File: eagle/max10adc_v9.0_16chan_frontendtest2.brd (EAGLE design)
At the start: 167 x 79 mm, 189 parts, among them IC1 MAX11115AUT+T, IC2 MAX11115AUT+T, IC3 OPA4322AIPWR, IC4 MAX11115AUT+T, IC5 MAX11115AUT+T, K1 AQY21SOP, K3 AQY21SOP, K5 AQY21SOP, K6 AQY21SOP, U340G CH340G, X1 LTI-SASF54GT, X4 LTI-SASF54GT, X5 LTI-SASF54GT, X6 LTI-SASF54GT, Y1 ABL-12.000MHZ-B2

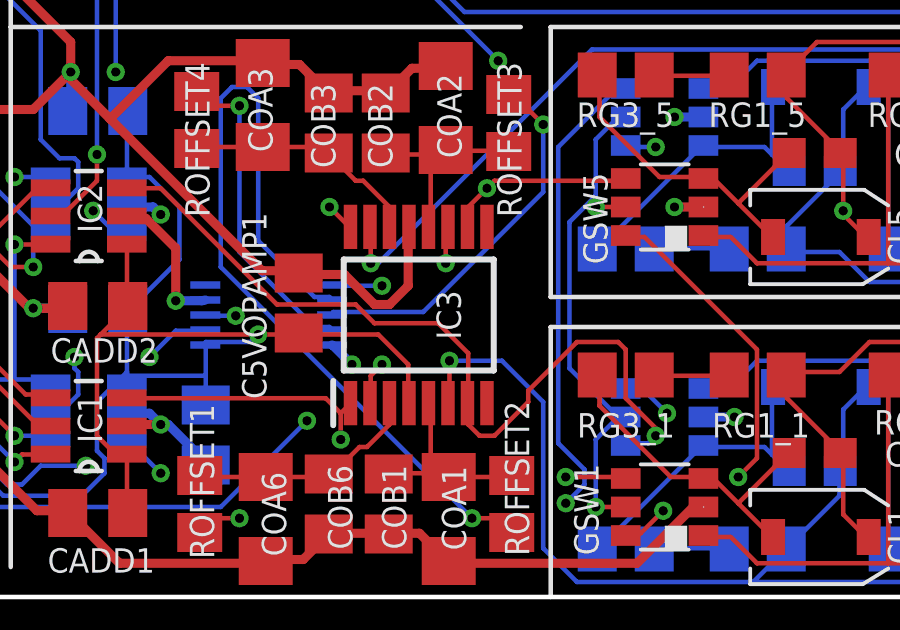
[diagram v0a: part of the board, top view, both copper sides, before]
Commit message: 2msps working
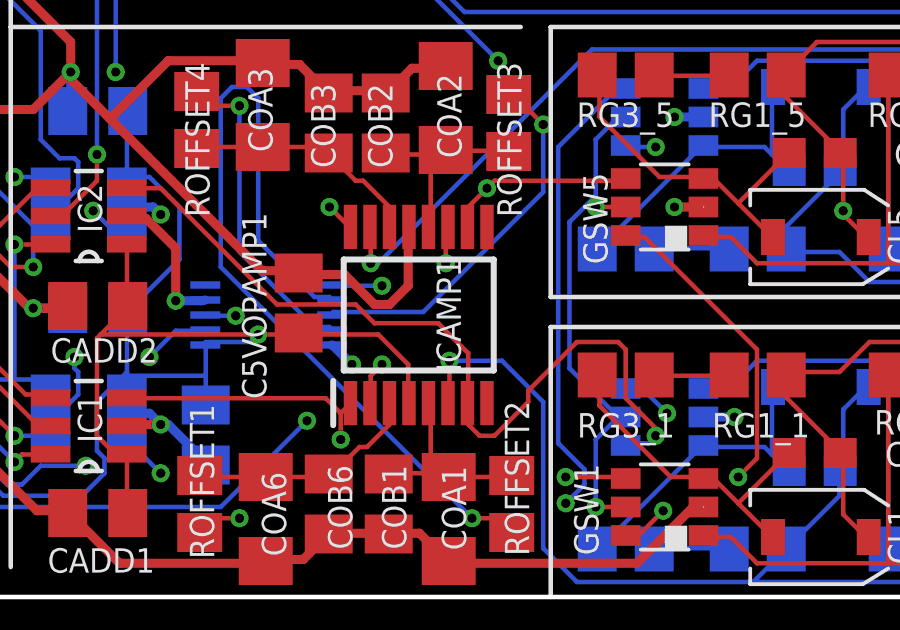
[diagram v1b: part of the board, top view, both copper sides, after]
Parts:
- removed IC5: MAX11115AUT+T, SamacSys_Parts:SOT95P280X145-6N
- added ICAMP1: OPA4322AIPWR, SamacSys_Parts:SOP65P640X120-16N
- IC3: value OPA4322AIPWR -> MAX11115AUT+T; device SamacSys_Parts:SOP65P640X120-16N -> SamacSys_Parts:SOT95P280X145-6N
- moved IC3 11.5 mm to (52.6, -5.80), flipped to the bottom, turned to 0 degrees
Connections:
- net CLKOUT_32: now also IC3.4; no longer IC5.4
- net CLKOUT_33: now also IC3.6; no longer IC5.6
- net D2A: now also IC3.5; no longer IC5.5
- net GND: now also IC3.2, ICAMP1.13; no longer IC3.13, IC5.2
- net INA1: now also ICAMP1.1; no longer IC3.1
- net INA2: now also ICAMP1.7; no longer IC3.7
- net INA3: now also IC3.3, ICAMP1.10; no longer IC3.10, IC5.3
- net INA4: now also ICAMP1.16; no longer IC3.16
- net INAMINUS1: now also ICAMP1.2; no longer IC3.2
- net INAMINUS2: now also ICAMP1.6; no longer IC3.6
- net INAMINUS3: now also ICAMP1.11; no longer IC3.11
- net INAMINUS4: now also ICAMP1.15; no longer IC3.15
- net OFFSET1: now also ICAMP1.3; no longer IC3.3
- net OFFSET2: now also ICAMP1.5; no longer IC3.5
- net OFFSET3: now also ICAMP1.12; no longer IC3.12
- net OFFSET4: now also ICAMP1.14; no longer IC3.14
- net VCCA: now also IC3.1, ICAMP1.4; no longer IC3.4, IC5.1
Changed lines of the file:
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@@
 <drawing>
 <settings>
-<setting alwaysvectorfont="yes"/>
+<setting alwaysvectorfont="no"/>
 <setting keepoldvectorfont="yes"/>
 <setting verticaltext="up"/>
@@
 <attribute name="NAME" x="45.4" y="58.75" size="0.8128" layer="25" ratio="18" rot="R180"/>
 </element>
-<element name="IC3" library="SamacSys_Parts" package="SOP65P640X120-16N" value="OPA4322AIPWR" x="63.6" y="-2.6" smashed="yes" rot="R90">
+<element name="ICAMP1" library="SamacSys_Parts" package="SOP65P640X120-16N" value="OPA4322AIPWR" x="63.6" y="-2.6" smashed="yes" rot="R90">
 <attribute name="DESCRIPTION" value="20MHz, Low Noise, 1.8V, RRIO, CMOS Operational Amplifier" x="63.6" y="-2.6" size="1.778" layer="27" rot="R90" display="off"/>
 <attribute name="HEIGHT" value="1.2mm" x="63.6" y="-2.6" size="1.778" layer="27" rot="R90" display="off"/>
@@
 <attribute name="NAME" x="54.9" y="5.175" size="0.8128" layer="26" font="vector" rot="MR0"/>
 </element>
-<element name="IC5" library="SamacSys_Parts" package="SOT95P280X145-6N" value="MAX11115AUT+T" x="52.6" y="-5.8" smashed="yes" rot="MR0">
+<element name="IC3" library="SamacSys_Parts" package="SOT95P280X145-6N" value="MAX11115AUT+T" x="52.6" y="-5.8" smashed="yes" rot="MR0">
 <attribute name="DESCRIPTION" value="ADC" x="56.6" y="-10.8" size="1.778" layer="28" rot="MR0" display="off"/>
 <attribute name="HEIGHT" value="mm" x="56.6" y="-10.8" size="1.778" layer="28" rot="MR0" display="off"/>
@@
 <contactref element="S1" pad="6"/>
 <contactref element="S2" pad="6"/>
-<contactref element="IC3" pad="13"/>
+<contactref element="ICAMP1" pad="13"/>
 <contactref element="IC4" pad="2"/>
 <contactref element="CADD1" pad="2"/>
@@
 <contactref element="IC2" pad="2"/>
 <contactref element="CADD3" pad="2"/>
-<contactref element="IC5" pad="2"/>
+<contactref element="IC3" pad="2"/>
 <contactref element="CADD4" pad="2"/>
 <contactref element="IOEXPAND_0X22" pad="10"/>
@@
 <contactref element="IC1" pad="6"/>
 <contactref element="IC2" pad="6"/>
-<contactref element="IC5" pad="6"/>
+<contactref element="IC3" pad="6"/>
 <wire x1="38.125" y1="18.75" x2="38.125" y2="19.375" width="0.1524" layer="1"/>
 <wire x1="37.5" y1="18.125" x2="38.125" y2="18.75" width="0.1524" layer="1"/>
@@
 <signal name="D2A">
 <contactref element="FPGA" pad="45"/>
-<contactref element="IC5" pad="5"/>
+<contactref element="IC3" pad="5"/>
 <wire x1="40.75" y1="25.5" x2="41.625" y2="25.5" width="0.1524" layer="1"/>
 <wire x1="42" y1="25.5" x2="40.75" y2="25.5" width="0.1524" layer="16"/>
@@
 <signal name="INA1">
 <contactref element="GSW1" pad="4"/>
-<contactref element="IC3" pad="1"/>
+<contactref element="ICAMP1" pad="1"/>
 <contactref element="IC1" pad="3"/>
 <wire x1="68.5" y1="-8" x2="70.5" y2="-8" width="0.1524" layer="1"/>
@@
 <contactref element="IC1" pad="4"/>
 <contactref element="IC2" pad="4"/>
-<contactref element="IC5" pad="4"/>
+<contactref element="IC3" pad="4"/>
 <wire x1="37.75" y1="20.25" x2="37.75" y2="19.5" width="0.1524" layer="1"/>
 <wire x1="37.875" y1="20.375" x2="37.75" y2="20.25" width="0.1524" layer="1"/>
@@
 <contactref element="RIN1" pad="2"/>
 <contactref element="CIN1" pad="2"/>
-<contactref element="IC3" pad="2"/>
+<contactref element="ICAMP1" pad="2"/>
 <wire x1="77.75" y1="-9.25" x2="77.75" y2="-7.25" width="0.1524" layer="1"/>
 <wire x1="78.5" y1="-10" x2="77.75" y2="-9.25" width="0.1524" layer="1"/>
@@
 <contactref element="ROFFSET1" pad="1"/>
 <contactref element="COA6" pad="2"/>
-<contactref element="IC3" pad="3"/>
+<contactref element="ICAMP1" pad="3"/>
 <wire x1="58.5" y1="-8" x2="56.375" y2="-8" width="0.1524" layer="1"/>
 <wire x1="56.375" y1="-8" x2="56.3" y2="-7.95" width="0.1524" layer="1"/>
@@
 <contactref element="DAC1" pad="1"/>
 <contactref element="COFFSET" pad="2"/>
-<contactref element="IC3" pad="4"/>
+<contactref element="ICAMP1" pad="4"/>
 <contactref element="IC4" pad="1"/>
 <contactref element="CADD1" pad="1"/>
@@
 <contactref element="IC2" pad="1"/>
 <contactref element="CADD3" pad="1"/>
-<contactref element="IC5" pad="1"/>
+<contactref element="IC3" pad="1"/>
 <contactref element="CADD4" pad="1"/>
 <wire x1="45.625" y1="1" x2="48.2" y2="1" width="0.1524" layer="1"/>
@@
 <signal name="INA2">
 <contactref element="GSW3" pad="4"/>
-<contactref element="IC3" pad="7"/>
+<contactref element="ICAMP1" pad="7"/>
 <contactref element="IC2" pad="3"/>
 <wire x1="71.25" y1="-6.875" x2="70.5" y2="-6.875" width="0.1524" layer="16"/>
@@
 <contactref element="RIN3" pad="2"/>
 <contactref element="CIN3" pad="2"/>
-<contactref element="IC3" pad="6"/>
+<contactref element="ICAMP1" pad="6"/>
 <wire x1="95.5" y1="-6.375" x2="95.5" y2="-8.75" width="0.1524" layer="16"/>
 <wire x1="95.5" y1="-8.75" x2="95.4" y2="-8.75" width="0.1524" layer="16"/>
@@
 <signal name="INA3">
 <contactref element="GSW5" pad="4"/>
-<contactref element="IC3" pad="10"/>
-<contactref element="IC5" pad="3"/>
+<contactref element="ICAMP1" pad="10"/>
+<contactref element="IC3" pad="3"/>
 <wire x1="66.125" y1="1.875" x2="70.5" y2="1.875" width="0.1524" layer="1"/>
 <wire x1="65.25" y1="1" x2="65.875" y2="1.625" width="0.1524" layer="1"/>
@@
 <contactref element="RIN5" pad="2"/>
 <contactref element="CIN5" pad="2"/>
-<contactref element="IC3" pad="11"/>
+<contactref element="ICAMP1" pad="11"/>
 <wire x1="95.5" y1="3.75" x2="95.5" y2="1.375" width="0.1524" layer="1"/>
 <wire x1="95.5" y1="1.375" x2="95.4" y2="1.35" width="0.1524" layer="1"/>
@@
 <signal name="INA4">
 <contactref element="GSW6" pad="4"/>
-<contactref element="IC3" pad="16"/>
+<contactref element="ICAMP1" pad="16"/>
 <contactref element="IC4" pad="3"/>
 <wire x1="71.5" y1="3" x2="70.5" y2="3" width="0.1524" layer="16"/>
@@
 <contactref element="RIN6" pad="2"/>
 <contactref element="CIN6" pad="2"/>
-<contactref element="IC3" pad="15"/>
+<contactref element="ICAMP1" pad="15"/>
 <wire x1="77.75" y1="4.25" x2="77.75" y2="2.25" width="0.1524" layer="16"/>
 <wire x1="78.5" y1="5" x2="77.75" y2="4.25" width="0.1524" layer="16"/>
@@
 <contactref element="COB3" pad="2"/>
 <contactref element="COA3" pad="2"/>
-<contactref element="IC3" pad="14"/>
+<contactref element="ICAMP1" pad="14"/>
 <wire x1="58.4" y1="3" x2="56.25" y2="3" width="0.1524" layer="1"/>
 <wire x1="56.25" y1="3" x2="56.2" y2="2.95" width="0.1524" layer="1"/>
@@
 <contactref element="COB2" pad="2"/>
 <contactref element="COA2" pad="2"/>
-<contactref element="IC3" pad="12"/>
+<contactref element="ICAMP1" pad="12"/>
 <wire x1="64" y1="2.375" x2="64" y2="0.375" width="0.1524" layer="1"/>
 <wire x1="64.5" y1="2.875" x2="64.375" y2="2.75" width="0.1524" layer="1"/>
@@
 <contactref element="COB1" pad="2"/>
 <contactref element="COA1" pad="2"/>
-<contactref element="IC3" pad="5"/>
+<contactref element="ICAMP1" pad="5"/>
 <wire x1="64" y1="-7.5" x2="64" y2="-5.625" width="0.1524" layer="1"/>
 <wire x1="64.5" y1="-8" x2="64.375" y2="-7.875" width="0.1524" layer="1"/>

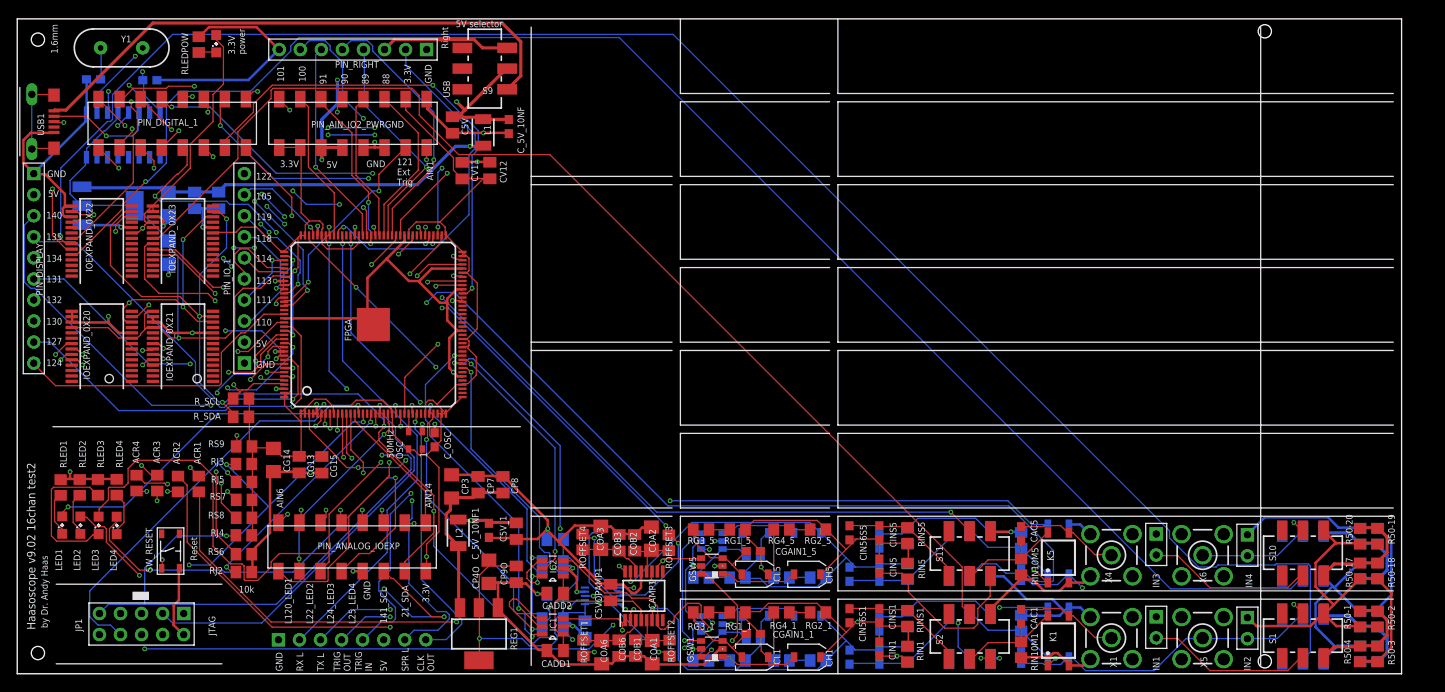
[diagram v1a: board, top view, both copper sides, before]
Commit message: 4x less gain and associated compensation, and input 6 pin connector
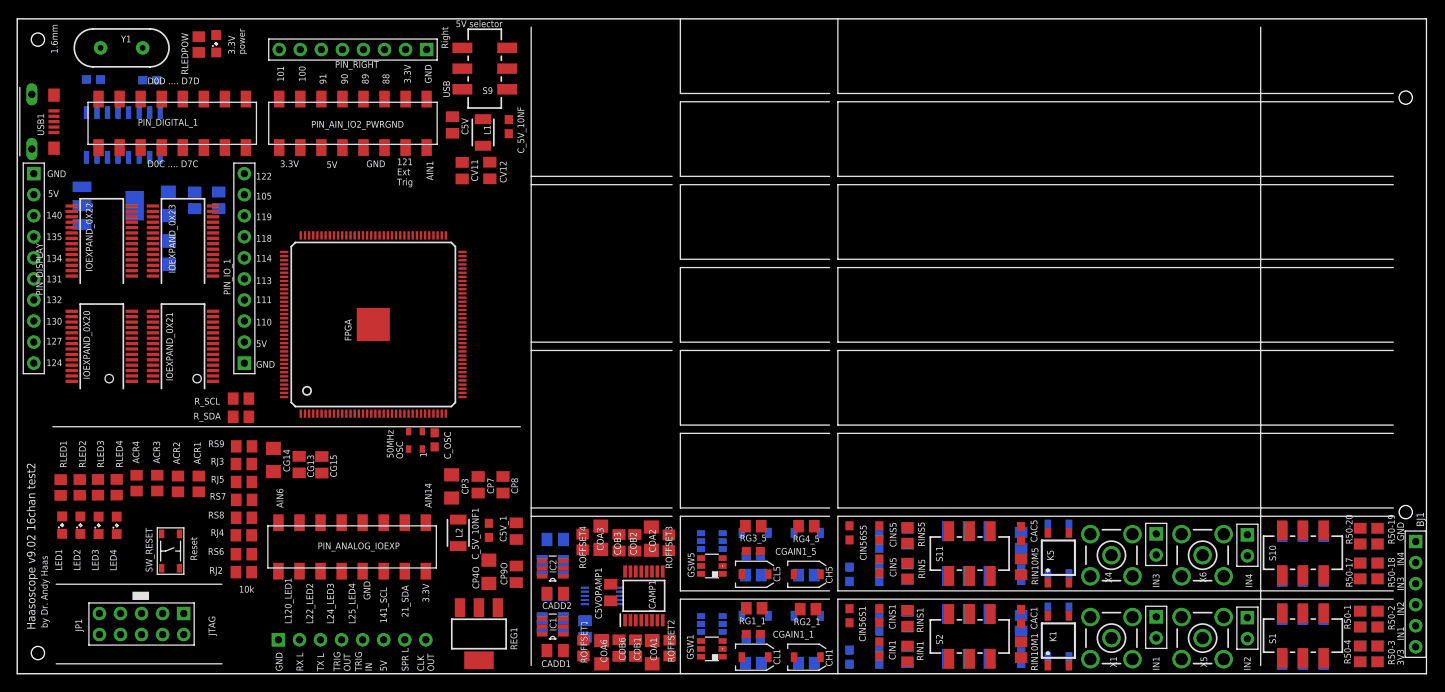
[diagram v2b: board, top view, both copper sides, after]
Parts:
- removed RG1_5, RG1_6, RG3_1, RG3_3: 100k, resistor:R0805
- removed RG2_5, RG2_6, RG4_1, RG4_3: 1M, resistor:R0805
- added BJ1: 6p-2.54, Seeed-Connector:H6-2.54
- CGAIN1_1, CGAIN1_3, CGAIN1_5, CGAIN1_6: value 33pF -> 220pF
- CH1, CH3, CH5, CH6: value 3-10pF -> 8-45pF
- RG1_1, RG1_3, RG3_5, RG3_6: value 100k -> 47k
- RG2_1, RG2_3, RG4_5, RG4_6: value 1M -> 470k
- moved RG3_5 6.31 mm to (76.8, 5.80)
- moved RG3_6 6.31 mm to (76.8, -0.10)
- moved RG4_5 3.03 mm to (83.2, 5.80)
- moved RG4_6 3.01 mm to (83.2, -0.10)
- moved RG1_1 2.06 mm to (76.9, -4.10)
- moved RG1_3 1.92 mm to (76.8, -10.7)
- moved RG2_3 1.43 mm to (83.2, -10.7)
- moved RG2_1 1.26 mm to (83.4, -4.20)
- moved S13 0.20 mm to (102.7, 2.50)
- moved S6 0.20 mm to (102.7, -7.50)
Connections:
- removed net INJ5: CAC5.2, IN3.2, K5.3, S10.2, X4.1
- removed net INJ6: CAC6.2, IN4.2, K6.3, S12.2, X6.1
- removed net N$2: RG1_1.1, RG3_1.2
- removed net N$20: RG1_5.1, RG3_5.2
- removed net N$21: RG2_5.1, RG4_5.2
- removed net N$25: RG1_6.1, RG3_6.2
- removed net N$26: RG2_6.1, RG4_6.2
- removed net N$3: RG2_1.1, RG4_1.2
- removed net N$7: RG1_3.1, RG3_3.2
- removed net N$8: RG2_3.1, RG4_3.2
- new net INJ2: BJ1.4, CAC3.2, IN2.2, K3.3, S5.2, X5.1
- new net INJ4: BJ1.2, CAC6.2, IN4.2, K6.3, S12.2, X6.1
- net CGAIN1: now also RG1_1.1; no longer RG3_1.1
- net CGAIN2: now also RG2_1.1; no longer RG4_1.1
- net CGAIN5: now also RG1_3.1; no longer RG3_3.1
- net CGAIN6: now also RG2_3.1; no longer RG4_3.1
- net GND: now also BJ1.1
- net INAMINUS3: now also RG3_5.2, RG4_5.2; no longer RG1_5.2, RG2_5.2
- net INAMINUS4: now also RG3_6.2, RG4_6.2; no longer RG1_6.2, RG2_6.2
- net INJ1: now also BJ1.5
- net INJ3: now also BJ1.3, CAC5.2, IN3.2, K5.3, S10.2, X4.1; no longer CAC3.2, IN2.2, K3.3, S5.2, X5.1
- net VCCA: now also BJ1.6
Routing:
- net GND: track 497.6 -> 0.00 mm, vias 33 -> 0
- net +3V3: track 364.8 -> 0.00 mm, vias 7 -> 0
- net E_50SW2: track 208.3 -> 0.00 mm, vias 1 -> 0
- net E_50SW3: track 198.9 -> 0.00 mm, vias 2 -> 0
- net E_50SW1: track 193.5 -> 0.00 mm, vias 2 -> 0
- net E_50SW4: track 192.3 -> 0.00 mm, vias 1 -> 0
- net +5V: track 163.8 -> 0.00 mm, vias 4 -> 0
- net L141_SCL: track 157.6 -> 0.00 mm, vias 8 -> 0
- net N$6: track 144.4 -> 0.00 mm, vias 2 -> 0
- net E_SS4: track 139.8 -> 0.00 mm, vias 2 -> 0
- net E_SS1: track 139.0 -> 0.00 mm
- net L21_SDA: track 138.6 -> 0.00 mm, vias 8 -> 0
- net N$5: track 138.0 -> 0.00 mm, vias 4 -> 0
- net N$11: track 128.0 -> 0.00 mm, vias 2 -> 0
- net N$4: track 127.4 -> 0.00 mm, vias 2 -> 0
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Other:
- board size 167 x 79 mm -> 170 x 79 mm
- board text added: "3V3"
- board text added: "D0C .... D7C"
- board text added: "D0D .... D7D"
- board text added: "IN1"
- board text added: "IN2"
- board text added: "IN3"
- board text added: "IN4"
